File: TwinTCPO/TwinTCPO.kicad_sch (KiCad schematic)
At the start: 44 parts, among them J1 Power, J2 Key, J3 Spk, J4 Phone, Q1 2N4401, Q2 2N7000, Q3 2N4401, Q4 2N4401, Q5 2N4403, U1 LM386

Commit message: Fix mounting hole clearance.
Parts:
- R6: value 10K -> 18K
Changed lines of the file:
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@@
       (effects (font (size 1.27 1.27)) (justify left))
     )
-    (property "Value" "10K" (id 1) (at 64.008 48.133 0)
+    (property "Value" "18K" (id 1) (at 64.008 48.133 0)
       (effects (font (size 1.27 1.27)) (justify left))
     )
@@
     )
     (path "/00000000-0000-0000-0000-000061703b08"
-      (reference "R6") (unit 1) (value "10K") (footprint "Resistor_THT:R_Axial_DIN0207_L6.3mm_D2.5mm_P10.16mm_Horizontal")
+      (reference "R6") (unit 1) (value "18K") (footprint "Resistor_THT:R_Axial_DIN0207_L6.3mm_D2.5mm_P10.16mm_Horizontal")
     )
     (path "/00000000-0000-0000-0000-0000616ff3fb"

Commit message: Change resistors for lower frequency
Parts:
- R2, R3: value 33K -> 47K
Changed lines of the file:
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@@
     (in_bom yes) (on_board yes)
     (property "Reference" "R2" (id 0) (at 27.94 86.1822 90))
-    (property "Value" "33K" (id 1) (at 27.94 88.4936 90))
+    (property "Value" "47K" (id 1) (at 27.94 88.4936 90))
     (property "Footprint" "Resistor_THT:R_Axial_DIN0207_L6.3mm_D2.5mm_P10.16mm_Horizontal" (id 2) (at 27.94 89.662 90)
       (effects (font (size 1.27 1.27)) hide)
@@
     (in_bom yes) (on_board yes)
     (property "Reference" "R3" (id 0) (at 43.18 86.1822 90))
-    (property "Value" "33K" (id 1) (at 43.18 88.4936 90))
+    (property "Value" "47K" (id 1) (at 43.18 88.4936 90))
     (property "Footprint" "Resistor_THT:R_Axial_DIN0207_L6.3mm_D2.5mm_P10.16mm_Horizontal" (id 2) (at 43.18 89.662 90)
       (effects (font (size 1.27 1.27)) hide)
@@
     )
     (path "/00000000-0000-0000-0000-00006174f21a"
-      (reference "R2") (unit 1) (value "33K") (footprint "Resistor_THT:R_Axial_DIN0207_L6.3mm_D2.5mm_P10.16mm_Horizontal")
+      (reference "R2") (unit 1) (value "47K") (footprint "Resistor_THT:R_Axial_DIN0207_L6.3mm_D2.5mm_P10.16mm_Horizontal")
     )
     (path "/00000000-0000-0000-0000-00006174fe32"
-      (reference "R3") (unit 1) (value "33K") (footprint "Resistor_THT:R_Axial_DIN0207_L6.3mm_D2.5mm_P10.16mm_Horizontal")
+      (reference "R3") (unit 1) (value "47K") (footprint "Resistor_THT:R_Axial_DIN0207_L6.3mm_D2.5mm_P10.16mm_Horizontal")
     )
     (path "/00000000-0000-0000-0000-000061757d40"

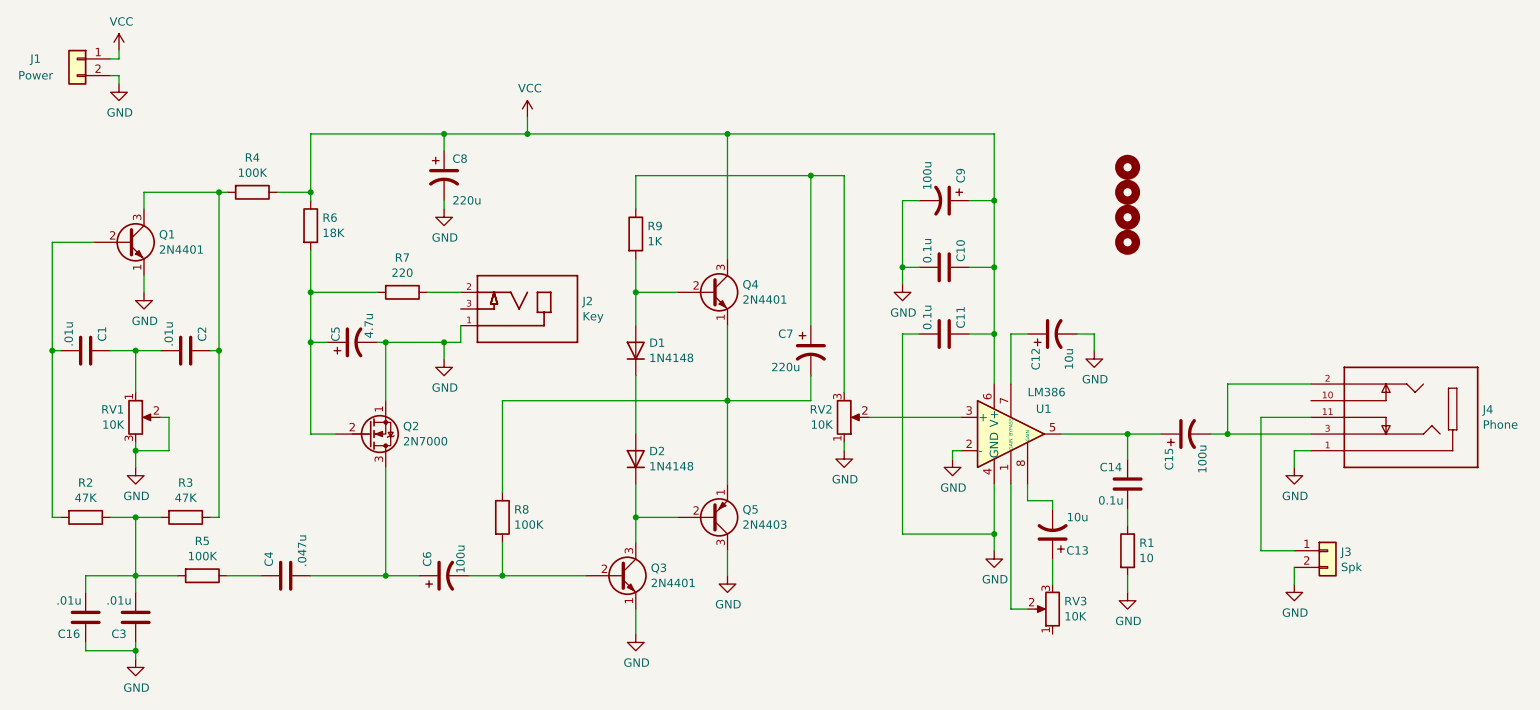
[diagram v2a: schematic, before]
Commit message: Start at version 2
* Remove headphone jack
* Change R2/R3 for lower frequency
* Add 2.2K resistor in series with RV1
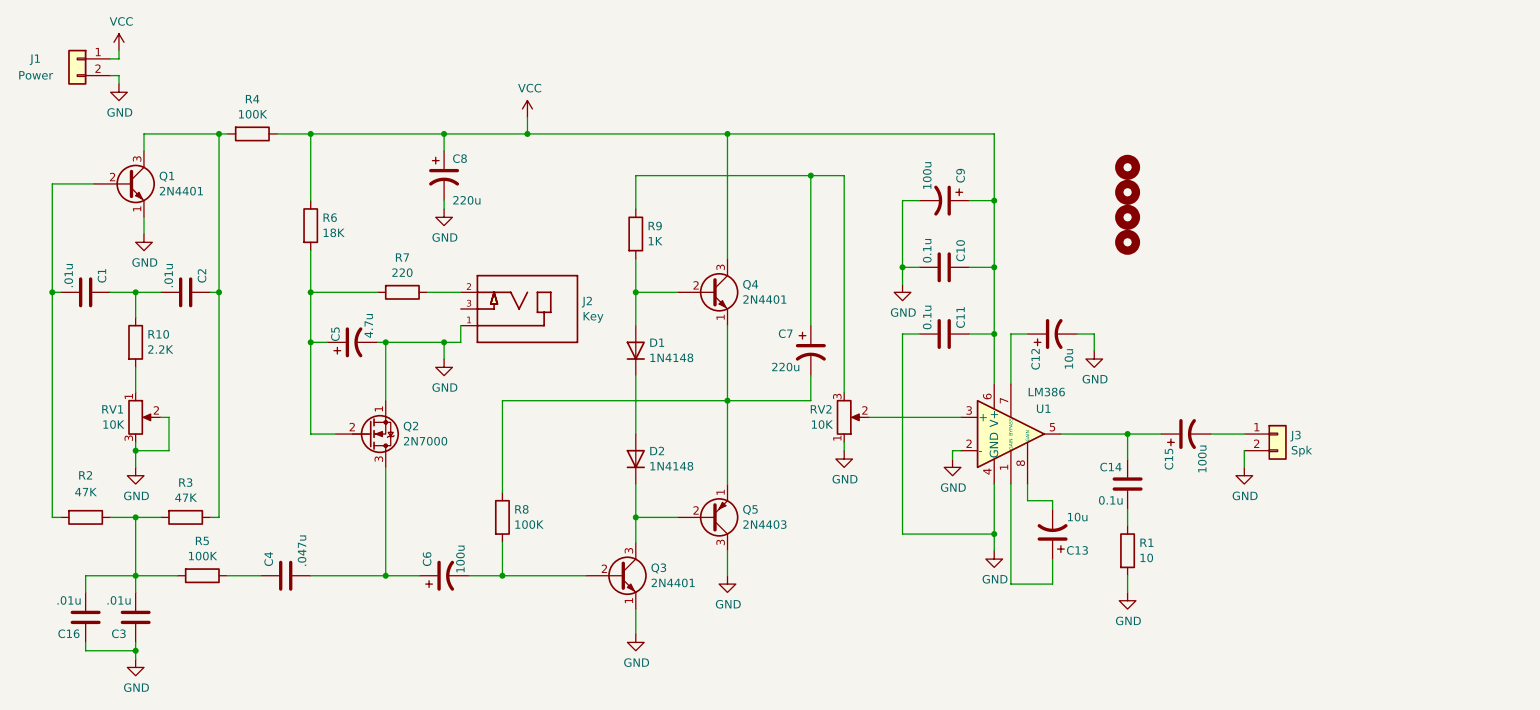
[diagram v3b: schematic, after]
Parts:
- removed J4: Phone, MyLibrary:CUI_SJ1-3525N, symbol SJ1-3525N:SJ1-3525N
- removed RV3: 10K, Potentiometer_THT:Potentiometer_Piher_PT-10-V10_Vertical, symbol Device:R_POT
- added R10: 2.2K, Resistor_THT:R_Axial_DIN0207_L6.3mm_D2.5mm_P2.54mm_Vertical, symbol Device:R
- C7, C8: footprint Capacitor_THT:CP_Radial_D8.0mm_P2.50mm -> Capacitor_THT:CP_Radial_D6.3mm_P2.50mm
- D1, D2: footprint Diode_THT:D_DO-35_SOD27_P10.16mm_Horizontal -> Diode_THT:D_DO-35_SOD27_P7.62mm_Horizontal
- R1, R2, R3, R4, R5, R6, R7, R8, R9: footprint Resistor_THT:R_Axial_DIN0207_L6.3mm_D2.5mm_P10.16mm_Horizontal -> Resistor_THT:R_Axial_DIN0207_L6.3mm_D2.5mm_P2.54mm_Vertical
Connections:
- net at U1.1 (GAIN): now also C13.1
- net at J3.1 (Pin_1): now also C15.2
- net at C1.1, C2.2: now also R10.1; no longer RV1.1
- new net: R10.2, RV1.1
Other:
- moved on the sheet: C1, C2, J3, Q1, R4
